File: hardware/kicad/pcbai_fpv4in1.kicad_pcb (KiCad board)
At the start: 6 copper layers, 50 x 50 mm, 253 parts, among them J1 BATT_PAD, J10 INA186A3IDCKR, J11 INA186A3IDCKR, J12 INA186A3IDCKR, J13 AT32F421K8T7, J14 DRV8300DRGER, J15 INA186A3IDCKR, J16 INA186A3IDCKR, J17 INA186A3IDCKR, J18 AT32F421K8T7, J19 DRV8300DRGER, J2 LMR51420YDDCR, J20 INA186A3IDCKR, J21 INA186A3IDCKR, J22 INA186A3IDCKR, J23 AT32F421K8T7, J24 DRV8300DRGER, J25 INA186A3IDCKR, J26 INA186A3IDCKR, J27 INA186A3IDCKR, J3 TLV76733DRVR, J4 SM08B-SRSS-TB, J5 USBLC6-2SC6, J6 USBLC6-2SC6, J7 USBLC6-2SC6, J8 AT32F421K8T7, J9 DRV8300DRGER, Q1 AON6260, Q10 AON6260, Q11 AON6260, Q12 AON6260, Q13 AON6260, Q14 AON6260, Q15 AON6260, Q16 AON6260, Q17 AON6260, Q18 AON6260, Q19 AON6260, Q2 AON6260, Q20 AON6260, Q21 AON6260, Q22 AON6260, Q23 AON6260, Q24 AON6260, Q25 AON6260, Q26 AON6260, Q27 AON6260, Q28 AON6260, Q3 AON6260, Q4 AON6260, Q5 AON6260, Q6 AON6260, Q7 AON6260, Q8 AON6260, Q9 AON6260

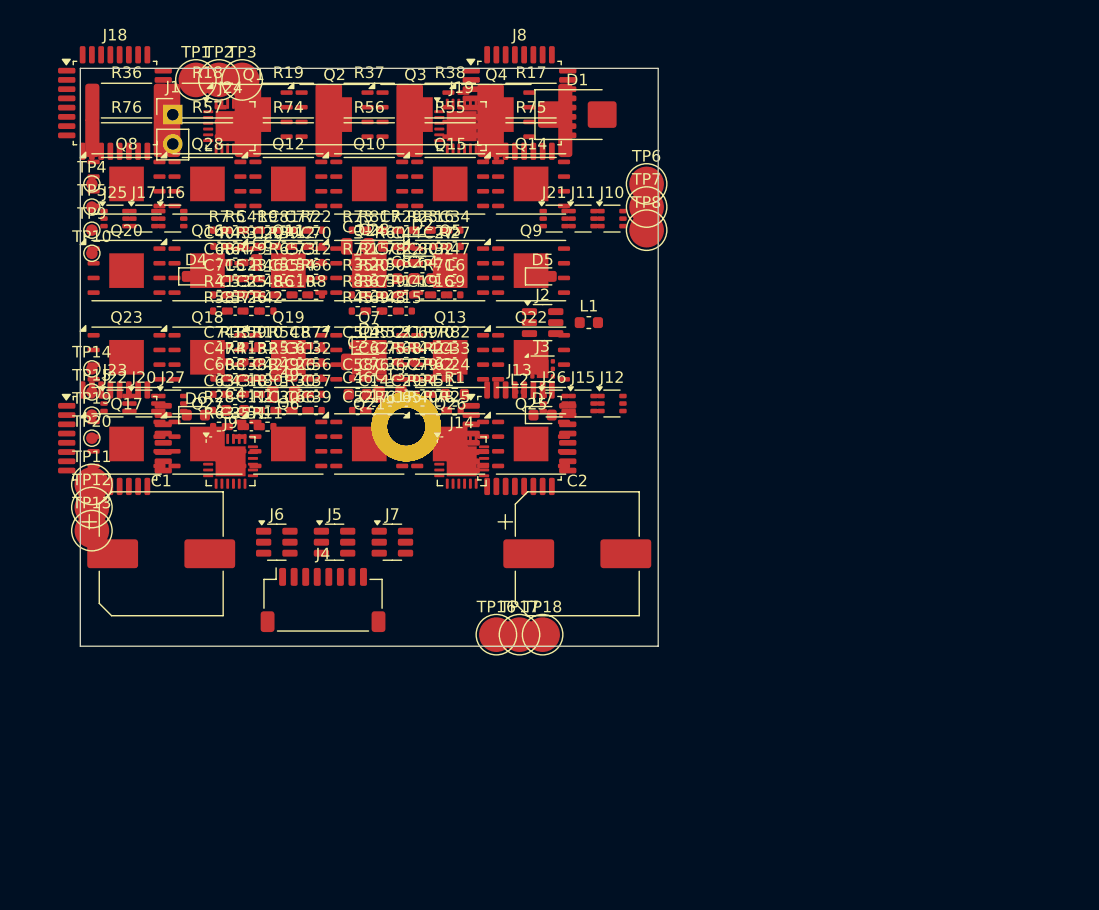
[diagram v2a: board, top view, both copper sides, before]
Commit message: Phase 4c-resume: Option C re-loop (TOLL + 85×70 board) CLOSES Phase 4
Sai's 2026-05-22 adjudication on Phase 4c blocker: Option C — engineering
rigor over target relaxation. 70 A continuous spec stays; increase board
size + use TOLL MOSFETs for lower R_thJC.

CHANGES (bundled re-loop of Phase 2b row + Phase 2.5 + Phase 4a + Phase 4b +
executes Phase 4c thermal sim in one PR per CLAUDE.md §6 worker-discretion
when one product-shape decision forces all):

Phase MOSFETs (24×): AON6260 DFN5x6 → AOTL66912 TOLL-8L
  - V_DS=100V over-spec (no penalty); 1.4mΩ typ; R_thJC=0.2°C/W (5× better)
  - 269A @ T_C=100°C; 100% UIS+Rg tested
  - JLC C3291324 ($2.51@1, $1.46@1k+, 2109 stock, Extended)

Reverse-polarity (4× AON6260): unchanged per Phase 2e.

Board form factor: 50×50 → 85×70 mm rectangular
  - B.Cu pure area grew 2.3× (1440 → 3245 mm²) due to TOLL footprint
  - 85×70 = 5950 mm² gives +24% B.Cu margin after 40% routing
  - 70×55 (master's starting suggestion) would have failed by 18%
  - Mount holes: 75×60 custom pattern (no standard FPV match; Sai accepts)

Heatsink: 46×32 → 80×55 mm Al6061 4mm, fin_mult 5× → 10×
TIM: 0.5mm silicone @ 4 W/m·K (conservative end of 4-6 datasheet range)

THERMAL SIM ENVELOPE 2 (THE CRITICAL GATE):
  R_thJC_parallel (24× TOLL) = 0.00833 °C/W
  R_thTIM = 0.0284 °C/W
  R_thHS_conv (h=80 + 10× fin × 44cm² slab) = 0.228 °C/W
  R_th_total = 0.27 °C/W
  P_board = 73.1 W (self-consistent at converged T_J)
  T_J = 79.8 °C  ← PASS (≤ 100 °C target, 20.2 °C margin) ✓

PHASE 5 ROUTING GATE CLEARED.

Master's h=80 W/m²·K design floor preserved (Rigor §2 — no goalpost moving).
70 A continuous spec preserved per Sai's direction.

Elmer FEM deferred to Phase 6 sim regime per Rigor §4 fallback — analytical
with locked Option C params is the trusted Phase 4c verdict. With 20°C
margin, Phase 9 bench validation is the next confidence step.

Files: hardware/kicad/{channel_skidl,setup_board,scripts/place_board}.py
       + .kicad_pcb regenerated end-to-end
     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
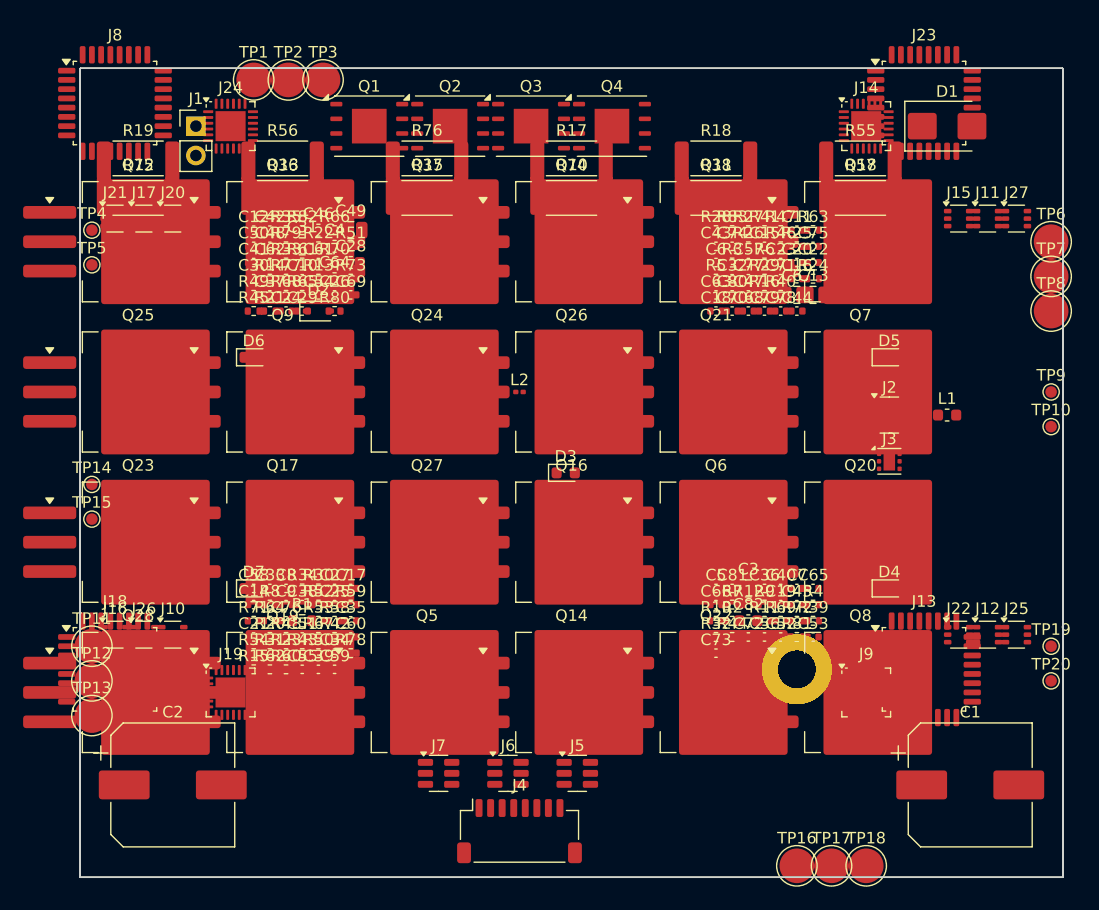
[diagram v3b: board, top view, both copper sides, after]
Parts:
- removed the ? at (28.2, 31.0) (x4)
- added ? (x12): , MountingHole:MountingHole_3.2mm_M3, F.Cu at (62.0, 52.0)
- Q10, Q11, Q12, Q13, Q14, Q15, Q16, Q17, Q18, Q19, Q20, Q21, Q22, Q23, Q24, Q25, Q26, Q27, Q28, Q5, Q6, Q7, Q8, Q9: value AON6260 -> AOTL66912; footprint Package_DFN_QFN:W-PDFN-8-1EP_6x5mm_P1.27mm_EP3x3mm -> Package_TO_SOT_SMD:TO-263-3_TabPin2
- moved J25 85.9 mm to (81.0, 49.0)
- moved TP20 85.6 mm to (84.0, 53.0)
- moved TP19 85.4 mm to (84.0, 50.0)
- moved TP10 84.3 mm to (84.0, 31.0)
- moved TP9 84.2 mm to (84.0, 28.0)
- moved Q8 77.3 mm to (67.5, 54.0)
- moved J23 75.8 mm to (73.0, 3.00)
- moved J22 75.7 mm to (76.0, 49.0)
- moved J27 74.7 mm to (81.0, 13.0)
- moved C1 72.8 mm to (77.0, 62.0)
- moved Q20 67.7 mm to (67.5, 41.0)
- moved D4 65.8 mm to (70.0, 45.0)
- moved J9 58.5 mm to (68.0, 54.0)
- moved C53 58.1 mm to (63.4, 49.2)
- moved Q18 57.4 mm to (67.5, 15.0)
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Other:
- board size 50 x 50 mm -> 85 x 70 mm

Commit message: Phase 4b-redo: connectivity-driven placement (per playbook trap T8)
Per Sai's feedback-redo-not-mitigate rule + playbook trap T8: re-do Phase 4b's
placement with per-MCU pin-side connectivity analysis BEFORE autoroute, not
after. Each channel's MCU is rotated so its PWM corner (chip's RIGHT+BOTTOM
corner = where PA8-10 PWM-HIGH on RIGHT + PA7/PB0/PB1 PWM-LOW on BOTTOM exit)
faces its inner direction toward the gate driver + MOSFETs.

LQFP-32 pin-side mapping fresh-read from AT32F421 DS Fig 3 p.20 (per Rigor §10
+ §5b — no recall). Per-channel rotations: CH1=0°, CH2=90°, CH3=270°, CH4=180°.

FET-to-channel re-grouping (same 24 (x,y) positions, different schematic-ref-
to-position assignment): rows-per-channel (60mm spread) → 3×2 corner sub-grids
(25×13mm cluster). Heatsink zone unchanged — Phase 4c thermal verdict preserved
(no Elmer re-run needed; symmetric N=24 parallel R_thJC model is unaffected).

Side-fix (R17 no loose threads): mount-hole bug caught during verification —
12 stacked at (62, 52) instead of 4 at proper corners. Two root causes:
(a) setup_board.py non-idempotent (appends 4 holes per run; 3 historical runs
→ 12), (b) place_board.py lib parser used re.match on block starting with
`\t(footprint ...` so leading tab made all mount holes mis-classified as
'passive' and collide at one position. Both fixed.

Verification (verify_placement.py NEW): 253 footprints placed; 24 phase MOSFETs
at expected 6×4 B.Cu grid; 4 MCUs at expected rotations; 4 mount holes at
proper corners; 12 motor pads on board edges; 0 overlaps.

Phase 5b autoroute is now expected as confirmation, not discovery — per playbook
T8 "route-validation must be a placement gate".

Co-Authored-By: Claude Opus 4.7 (1M context) <noreply@anthropic.com>
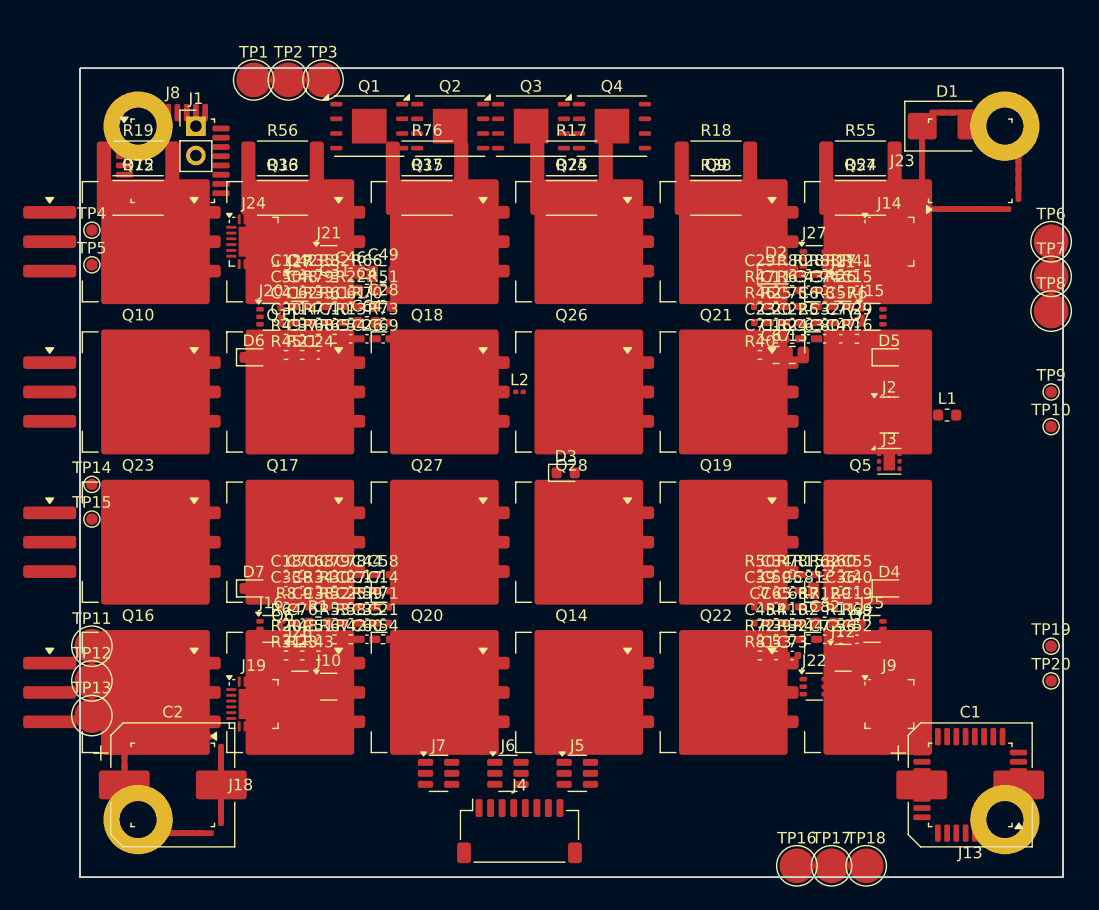
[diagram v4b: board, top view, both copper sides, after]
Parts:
- removed the ? at (62.0, 52.0) (x12)
- added ?: , MountingHole:MountingHole_3.2mm_M3, F.Cu at (5.00, 5.00)
- added ?: , MountingHole:MountingHole_3.2mm_M3, F.Cu at (80.0, 5.00)
- added ?: , MountingHole:MountingHole_3.2mm_M3, F.Cu at (5.00, 65.0)
- added ?: , MountingHole:MountingHole_3.2mm_M3, F.Cu at (80.0, 65.0)
- moved R62 48.7 mm to (64.4, 43.8)
- moved C55 48.7 mm to (67.2, 43.8)
- moved R15 48.7 mm to (63.0, 43.8)
- moved R60 48.7 mm to (65.8, 43.8)
- moved C18 43.6 mm to (17.8, 43.8)
- moved C44 43.6 mm to (24.8, 43.8)
- moved C70 43.6 mm to (19.2, 43.8)
- moved C78 43.6 mm to (23.4, 43.8)
- moved C79 43.6 mm to (22.0, 43.8)
- moved C68 43.6 mm to (20.6, 43.8)
- moved D2 39.7 mm to (60.2, 17.8)
- moved R80 39.7 mm to (61.6, 17.8)
- moved C29 39.7 mm to (58.8, 17.8)
- moved Q10 39.7 mm to (5.00, 28.0)
- moved Q11 39.7 mm to (17.5, 28.0)
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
